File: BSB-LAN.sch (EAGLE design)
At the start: 20 parts, among them Q1 BC847, Q2 BC857

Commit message: Add OSHW Logo
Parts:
- added U$3: OSHW-LOGOM, BSB-LAN:OSHW-LOGOM
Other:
- moved on the sheet: C1, UEXT
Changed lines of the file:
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@@
 <layer number="59" name="tCarbon" color="7" fill="1" visible="no" active="no"/>
 <layer number="60" name="bCarbon" color="7" fill="1" visible="no" active="no"/>
+<layer number="88" name="SimResults" color="9" fill="1" visible="yes" active="yes"/>
+<layer number="89" name="SimProbes" color="9" fill="1" visible="yes" active="yes"/>
 <layer number="90" name="Modules" color="7" fill="1" visible="yes" active="yes"/>
 <layer number="91" name="Nets" color="2" fill="1" visible="yes" active="yes"/>
@@
 <attribute name="LCSC_PART" value="C17888"/>
 </part>
+<part name="U$3" library="BSB-LAN" deviceset="OSHW-LOGO" device="M"/>
 </parts>
 <sheets>
@@
 <attribute name="LCSC_PART" x="170.18" y="144.78" size="1.4224" layer="96" font="vector" ratio="10" rot="MR0" align="center" display="off"/>
 </instance>
-<instance part="UEXT" gate="G$1" x="223.52" y="48.26" rot="R180"/>
+<instance part="UEXT" gate="G$1" x="223.52" y="58.42" rot="R180"/>
 <instance part="D1" gate="G$1" x="124.46" y="99.06" rot="R270">
 <attribute name="LCSC_PART" x="124.46" y="99.06" size="1.4224" layer="96" font="vector" ratio="10" rot="R270" align="center" display="off"/>
@@
 <attribute name="LCSC_PART" x="104.14" y="127" size="2.54" layer="96" font="vector" ratio="10" rot="MR270" align="center" display="off"/>
 </instance>
-<instance part="C1" gate="G$1" x="175.26" y="50.8">
-<attribute name="LCSC_PART" x="175.26" y="50.8" size="2.54" layer="96" font="vector" ratio="10" align="center" display="off"/>
+<instance part="C1" gate="G$1" x="175.26" y="60.96">
+<attribute name="LCSC_PART" x="175.26" y="60.96" size="2.54" layer="96" font="vector" ratio="10" align="center" display="off"/>
 </instance>
 <instance part="D3" gate="G$2" x="58.42" y="106.68" rot="R90">
@@
 <attribute name="LCSC_PART" x="71.12" y="116.84" size="2.54" layer="96" font="vector" ratio="10" align="center" display="off"/>
 </instance>
+<instance part="U$3" gate="G$1" x="241.3" y="35.56"/>
 </instances>
 <busses>
@@
 </segment>
 <segment>
-<wire x1="175.26" y1="43.18" x2="182.88" y2="43.18" width="0.1524" layer="91"/>
-<label x="182.88" y="43.18" size="1.4224" layer="95" font="vector" ratio="10" rot="MR180" xref="yes"/>
+<wire x1="175.26" y1="53.34" x2="182.88" y2="53.34" width="0.1524" layer="91"/>
+<label x="182.88" y="53.34" size="1.4224" layer="95" font="vector" ratio="10" rot="MR180" xref="yes"/>
 <pinref part="C1" gate="G$1" pin="2"/>
-<wire x1="175.26" y1="45.72" x2="175.26" y2="43.18" width="0.1524" layer="91"/>
-</segment>
-<segment>
-<wire x1="231.14" y1="53.34" x2="238.76" y2="53.34" width="0.1524" layer="91"/>
-<label x="238.76" y="53.34" size="1.4224" layer="95" font="vector" ratio="10" rot="MR180" xref="yes"/>
+<wire x1="175.26" y1="55.88" x2="175.26" y2="53.34" width="0.1524" layer="91"/>
+</segment>
+<segment>
+<wire x1="231.14" y1="63.5" x2="238.76" y2="63.5" width="0.1524" layer="91"/>
+<label x="238.76" y="63.5" size="1.4224" layer="95" font="vector" ratio="10" rot="MR180" xref="yes"/>
 <pinref part="UEXT" gate="G$1" pin="2"/>
 </segment>
@@
 </segment>
 <segment>
-<wire x1="175.26" y1="55.88" x2="182.88" y2="55.88" width="0.1524" layer="91"/>
-<label x="182.88" y="55.88" size="1.4224" layer="95" font="vector" ratio="10" rot="MR180" xref="yes"/>
+<wire x1="175.26" y1="66.04" x2="182.88" y2="66.04" width="0.1524" layer="91"/>
+<label x="182.88" y="66.04" size="1.4224" layer="95" font="vector" ratio="10" rot="MR180" xref="yes"/>
 <pinref part="C1" gate="G$1" pin="1"/>
-<wire x1="175.26" y1="55.88" x2="175.26" y2="53.34" width="0.1524" layer="91"/>
-</segment>
-<segment>
-<wire x1="215.9" y1="53.34" x2="208.28" y2="53.34" width="0.1524" layer="91"/>
-<label x="208.28" y="53.34" size="1.4224" layer="95" font="vector" ratio="10" rot="MR0" xref="yes"/>
+<wire x1="175.26" y1="66.04" x2="175.26" y2="63.5" width="0.1524" layer="91"/>
+</segment>
+<segment>
+<wire x1="215.9" y1="63.5" x2="208.28" y2="63.5" width="0.1524" layer="91"/>
+<label x="208.28" y="63.5" size="1.4224" layer="95" font="vector" ratio="10" rot="MR0" xref="yes"/>
 <pinref part="UEXT" gate="G$1" pin="1"/>
 </segment>
@@
 </segment>
 <segment>
-<label x="208.28" y="50.8" size="1.4224" layer="95" font="vector" ratio="10" rot="R180" xref="yes"/>
-<wire x1="215.9" y1="50.8" x2="208.28" y2="50.8" width="0.1524" layer="91"/>
+<label x="208.28" y="60.96" size="1.4224" layer="95" font="vector" ratio="10" rot="R180" xref="yes"/>
+<wire x1="215.9" y1="60.96" x2="208.28" y2="60.96" width="0.1524" layer="91"/>
 <pinref part="UEXT" gate="G$1" pin="3"/>
 </segment>
@@
 </segment>
 <segment>
-<wire x1="231.14" y1="50.8" x2="238.76" y2="50.8" width="0.1524" layer="91"/>
-<label x="238.76" y="50.8" size="1.4224" layer="95" font="vector" ratio="10" xref="yes"/>
+<wire x1="231.14" y1="60.96" x2="238.76" y2="60.96" width="0.1524" layer="91"/>
+<label x="238.76" y="60.96" size="1.4224" layer="95" font="vector" ratio="10" xref="yes"/>
 <pinref part="UEXT" gate="G$1" pin="4"/>
 </segment>
@@
 <net name="SCL" class="0">
 <segment>
-<wire x1="215.9" y1="48.26" x2="208.28" y2="48.26" width="0.1524" layer="91"/>
-<label x="208.28" y="48.26" size="1.4224" layer="95" font="vector" ratio="10" rot="MR0" xref="yes"/>
+<wire x1="215.9" y1="58.42" x2="208.28" y2="58.42" width="0.1524" layer="91"/>
+<label x="208.28" y="58.42" size="1.4224" layer="95" font="vector" ratio="10" rot="MR0" xref="yes"/>
 <pinref part="UEXT" gate="G$1" pin="5"/>
 </segment>
@@
 <net name="SDA" class="0">
 <segment>
-<wire x1="231.14" y1="48.26" x2="238.76" y2="48.26" width="0.1524" layer="91"/>
-<label x="238.76" y="48.26" size="1.4224" layer="95" font="vector" ratio="10" rot="MR180" xref="yes"/>
+<wire x1="231.14" y1="58.42" x2="238.76" y2="58.42" width="0.1524" layer="91"/>
+<label x="238.76" y="58.42" size="1.4224" layer="95" font="vector" ratio="10" rot="MR180" xref="yes"/>
 <pinref part="UEXT" gate="G$1" pin="6"/>
 </segment>
@@
 <net name="MISO" class="0">
 <segment>
-<wire x1="215.9" y1="45.72" x2="208.28" y2="45.72" width="0.1524" layer="91"/>
-<label x="208.28" y="45.72" size="1.4224" layer="95" font="vector" ratio="10" rot="MR0" xref="yes"/>
+<wire x1="215.9" y1="55.88" x2="208.28" y2="55.88" width="0.1524" layer="91"/>
+<label x="208.28" y="55.88" size="1.4224" layer="95" font="vector" ratio="10" rot="MR0" xref="yes"/>
 <pinref part="UEXT" gate="G$1" pin="7"/>
 </segment>
@@
 <net name="MOSI" class="0">
 <segment>
-<wire x1="231.14" y1="45.72" x2="238.76" y2="45.72" width="0.1524" layer="91"/>
-<label x="238.76" y="45.72" size="1.4224" layer="95" font="vector" ratio="10" rot="MR180" xref="yes"/>
+<wire x1="231.14" y1="55.88" x2="238.76" y2="55.88" width="0.1524" layer="91"/>
+<label x="238.76" y="55.88" size="1.4224" layer="95" font="vector" ratio="10" rot="MR180" xref="yes"/>
 <pinref part="UEXT" gate="G$1" pin="8"/>
 </segment>
@@
 <net name="SCK" class="0">
 <segment>
-<wire x1="215.9" y1="43.18" x2="208.28" y2="43.18" width="0.1524" layer="91"/>
-<label x="208.28" y="43.18" size="1.4224" layer="95" font="vector" ratio="10" rot="MR0" xref="yes"/>
+<wire x1="215.9" y1="53.34" x2="208.28" y2="53.34" width="0.1524" layer="91"/>
+<label x="208.28" y="53.34" size="1.4224" layer="95" font="vector" ratio="10" rot="MR0" xref="yes"/>
 <pinref part="UEXT" gate="G$1" pin="9"/>
 </segment>
@@
 <net name="SSEL" class="0">
 <segment>
-<wire x1="231.14" y1="43.18" x2="238.76" y2="43.18" width="0.1524" layer="91"/>
-<label x="238.76" y="43.18" size="1.4224" layer="95" font="vector" ratio="10" rot="MR180" xref="yes"/>
+<wire x1="231.14" y1="53.34" x2="238.76" y2="53.34" width="0.1524" layer="91"/>
+<label x="238.76" y="53.34" size="1.4224" layer="95" font="vector" ratio="10" rot="MR180" xref="yes"/>
 <pinref part="UEXT" gate="G$1" pin="10"/>
 </segment>

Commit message: Update Libraries in basic BSB-LAN design
Bring up to date with JLC export attributes.
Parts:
- U$3: value OSHW-LOGOM -> DNI
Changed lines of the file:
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@@
 <attribute name="LCSC_PART" value="C17888"/>
 </part>
-<part name="U$3" library="BSB-LAN" deviceset="OSHW-LOGO" device="M"/>
+<part name="U$3" library="BSB-LAN" deviceset="OSHW-LOGO" device="M" value="DNI"/>
 </parts>
 <sheets>

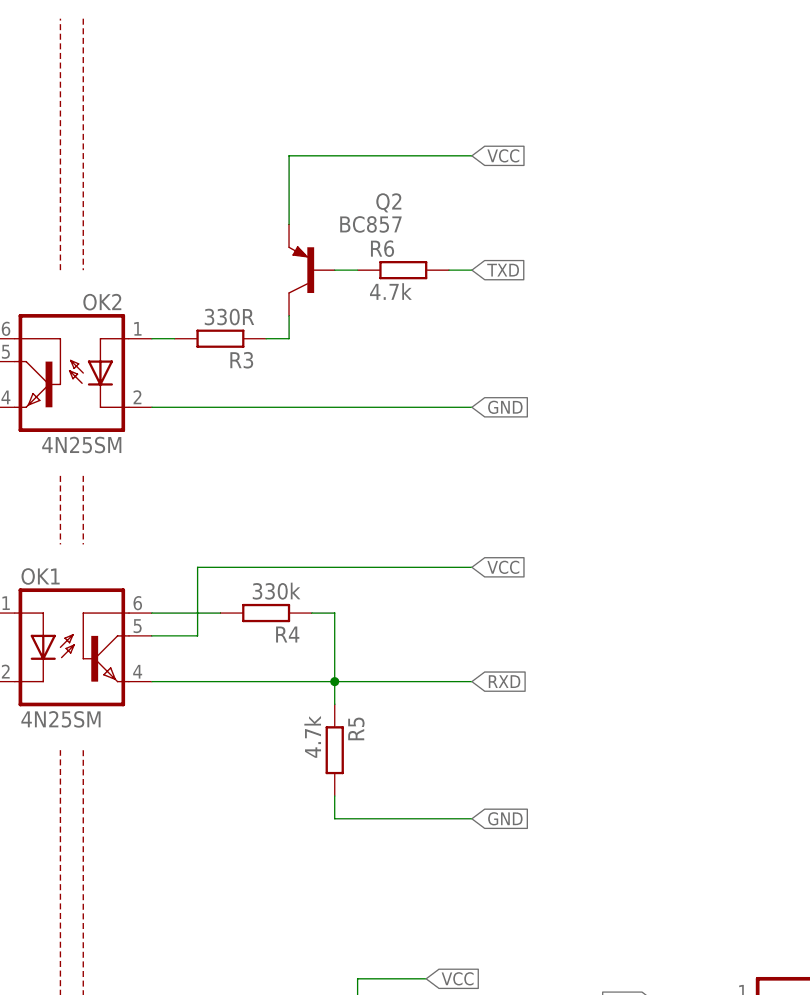
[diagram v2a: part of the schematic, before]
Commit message: Add missing pull-down to BSB-LAN adapter
4.7k on the TX pin to assist with boot issues on the Olimex dev kit.
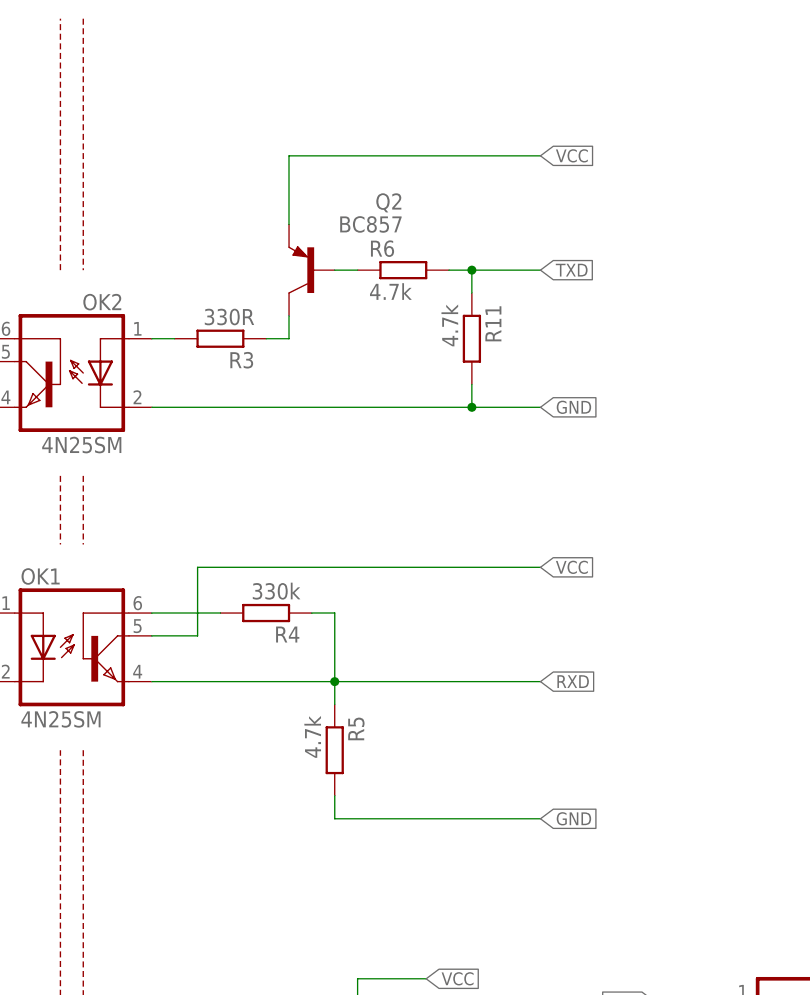
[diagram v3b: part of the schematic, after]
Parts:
- added R11: 4.7k, BSB-LAN:R-EU_R0805L
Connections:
- net GND: now also R11.2
- net TXD: now also R11.1
